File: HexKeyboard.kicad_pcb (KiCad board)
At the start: 2 copper layers, 66.8 x 99.3 mm, 37 parts, among them J3 Conn_02x04_Odd_Even, J5 USB_A, SW1 SW_3, SW10 SW_9, SW11 SW_8, SW12 SW_7, SW13 SW_Hash, SW14 SW_Hash, SW15 SW_0, SW16 SW_Star, SW17 SW_Hash, SW18 SW_Hash, SW19 SW_0, SW2 SW_3, SW20 SW_Star, SW3 SW_2, SW4 SW_1, SW5 SW_6, SW6 SW_6, SW7 SW_5, SW8 SW_4, SW9 SW_9, U2 74LVC125, U4 AT24CS64-XHM, Y1 16MHz

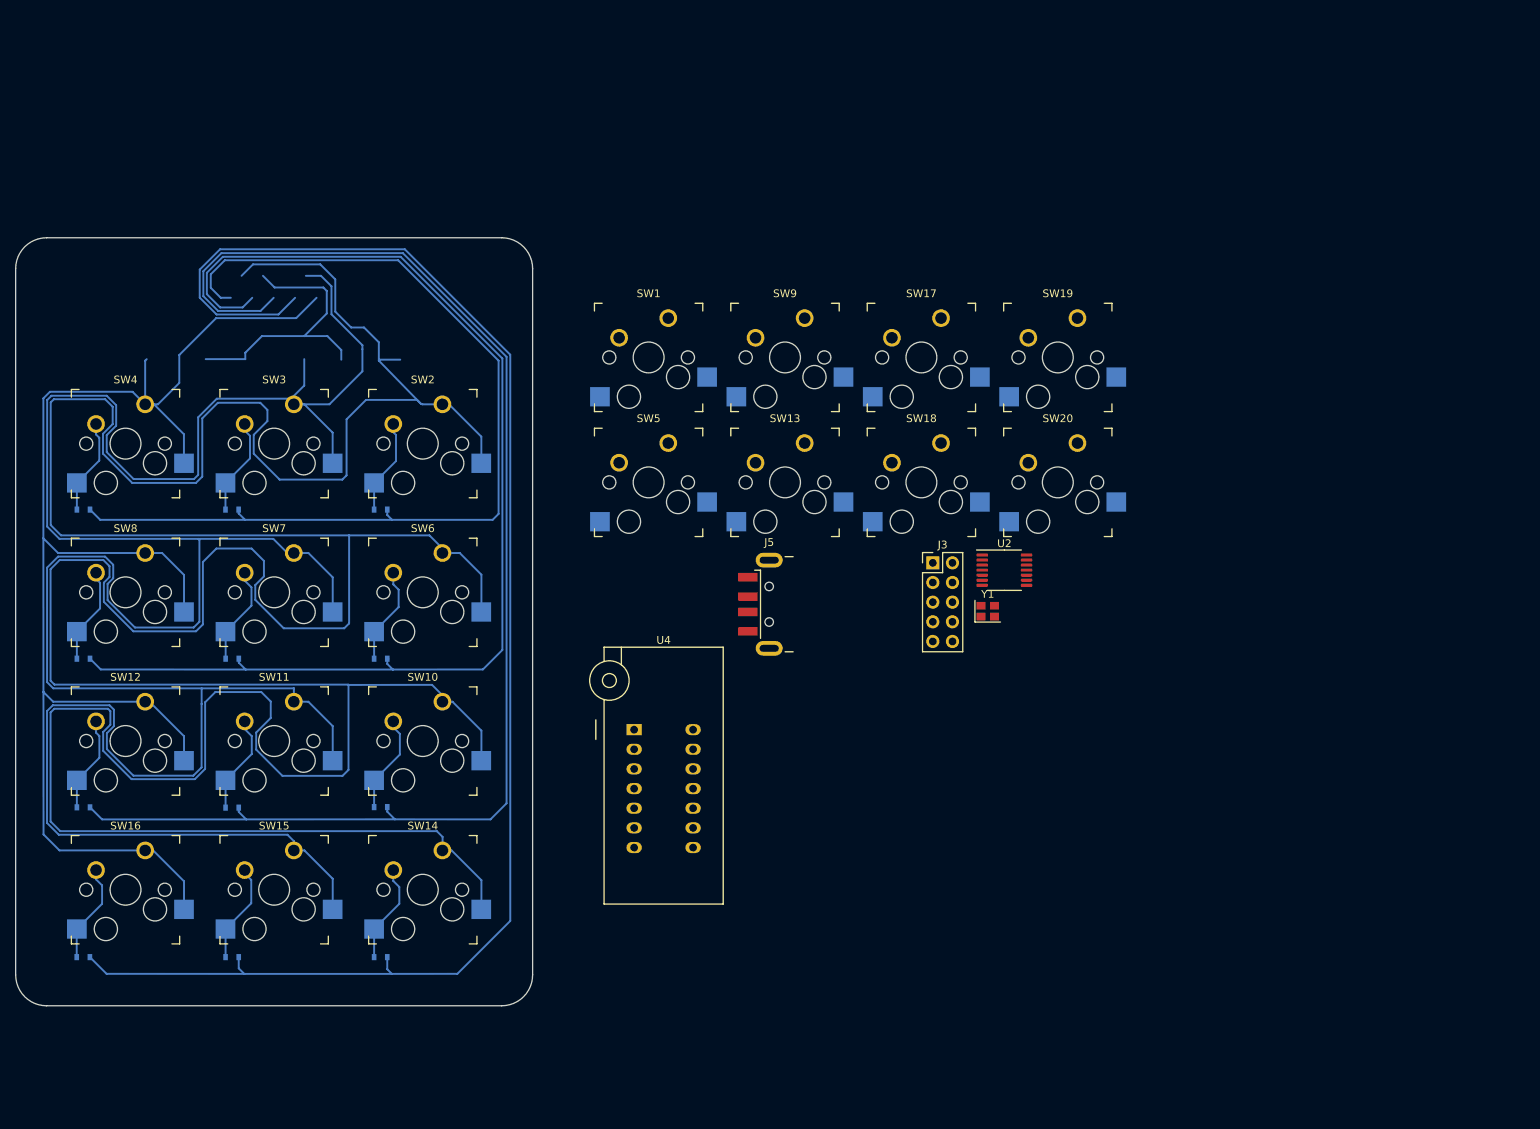
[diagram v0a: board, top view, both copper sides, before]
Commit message: Cleaned up libraries Added Display Switched to USB-C
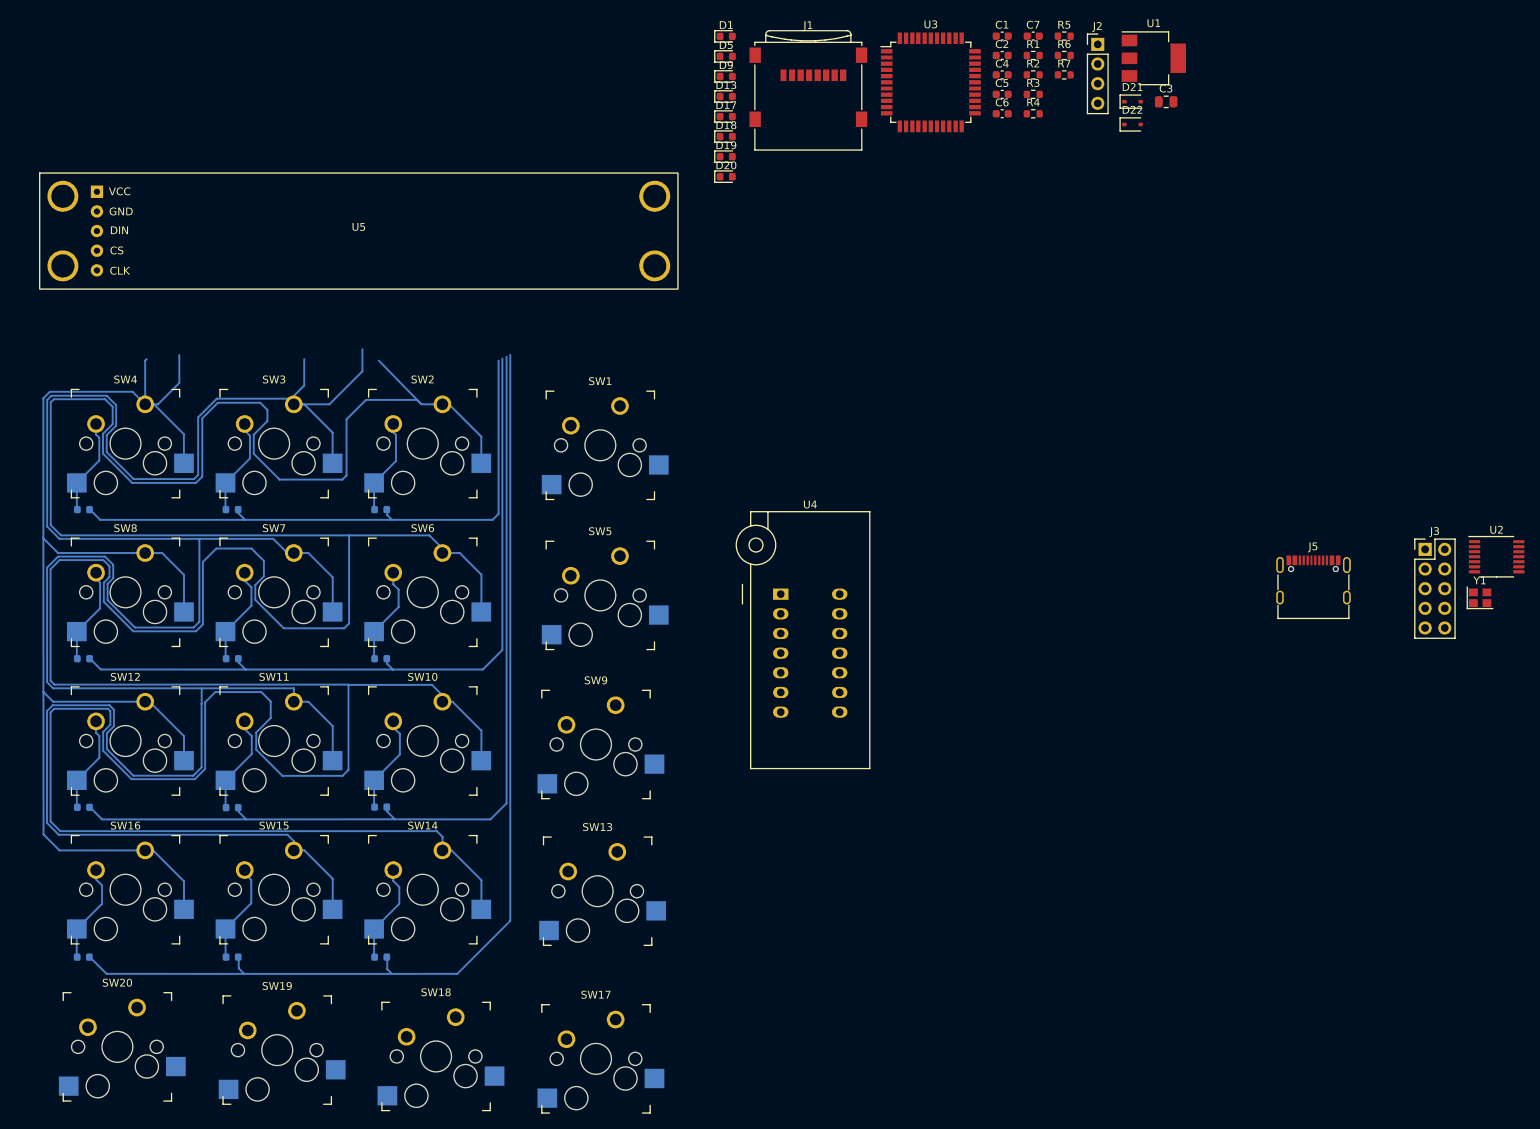
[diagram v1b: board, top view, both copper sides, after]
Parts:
- added C1: 100nF, Capacitor_SMD:C_0603_1608Metric, F.Cu at (209.5, 34.6)
- added C2: 100nF, Capacitor_SMD:C_0603_1608Metric, F.Cu at (209.5, 37.2)
- added C3: 10uF/10V, Capacitor_SMD:C_0805_2012Metric, F.Cu at (230.7, 43.1)
- added C4: 100nF, Capacitor_SMD:C_0603_1608Metric, F.Cu at (209.5, 39.7)
- added C5: 9pF, Capacitor_SMD:C_0603_1608Metric, F.Cu at (209.5, 42.2)
- added C6: 9pF, Capacitor_SMD:C_0603_1608Metric, F.Cu at (209.5, 44.7)
- added C7: 1uF, Capacitor_SMD:C_0603_1608Metric, F.Cu at (213.5, 34.6)
- added D1: D, Diode_SMD:D_0603_1608Metric, F.Cu at (173.9, 34.7)
- added D13: D, Diode_SMD:D_0603_1608Metric, F.Cu at (173.9, 42.5)
- added D17: D, Diode_SMD:D_0603_1608Metric, F.Cu at (173.9, 45.0)
- added D18: D, Diode_SMD:D_0603_1608Metric, F.Cu at (173.9, 47.6)
- added D19: D, Diode_SMD:D_0603_1608Metric, F.Cu at (173.9, 50.2)
- added D20: D, Diode_SMD:D_0603_1608Metric, F.Cu at (173.9, 52.8)
- added D21: BZX384-xxx, Diode_SMD:D_SOD-323, F.Cu at (226.4, 43.1)
- added D22: BZX384-xxx, Diode_SMD:D_SOD-323, F.Cu at (226.4, 46.1)
- added D5: D, Diode_SMD:D_0603_1608Metric, F.Cu at (173.9, 37.3)
- added D9: D, Diode_SMD:D_0603_1608Metric, F.Cu at (173.9, 39.9)
- added J1: Micro_SD_Card, Connector_Card:microSD_HC_Wuerth_693072010801, F.Cu at (184.5, 41.3)
- added J2: Conn_01x04, Connector_PinHeader_2.54mm:PinHeader_1x04_P2.54mm_Vertical, F.Cu at (221.9, 35.7)
- added R1: 3k3, Resistor_SMD:R_0603_1608Metric, F.Cu at (213.5, 37.2)
- added R2: 3k3, Resistor_SMD:R_0603_1608Metric, F.Cu at (213.5, 39.7)
- added R3: 3k3, Resistor_SMD:R_0603_1608Metric, F.Cu at (213.5, 42.2)
- added R4: 22, Resistor_SMD:R_0603_1608Metric, F.Cu at (213.5, 44.7)
- added R5: 22, Resistor_SMD:R_0603_1608Metric, F.Cu at (217.5, 34.6)
- added R6: 5k6, Resistor_SMD:R_0603_1608Metric, F.Cu at (217.5, 37.2)
- added R7: 5k6, Resistor_SMD:R_0603_1608Metric, F.Cu at (217.5, 39.7)
- added U1: AMS1117-3.3, Package_TO_SOT_SMD:SOT-223-3_TabPin2, F.Cu at (229.1, 37.5)
- added U3: ATmega32U4-AU, Package_QFP:TQFP-44_10x10mm_P0.8mm, F.Cu at (200.3, 40.6)
- added U5: MAX7219, MyFootprints:Display_x8_MAX7219, F.Cu at (126.4, 59.8)
- D10, D11, D12, D14, D15, D16, D2, D3, D4, D6, D7, D8: footprint Diodes_SMD:D_0603 -> Diode_SMD:D_0603_1608Metric
- J5: footprint Connector_USB:USB_A_CNCTech_1001-011-01101_Horizontal -> Connector_USB:USB_C_Receptacle_G-Switch_GT-USB-7010ASV
- moved SW20 141.8 mm to (97.7, 160.2)
- moved SW19 134.9 mm to (118.4, 160.6)
- moved SW17 99.9 mm to (159.6, 161.8)
- moved SW18 97.2 mm to (138.9, 161.4)
- moved Y1 63.7 mm to (271.3, 107.2)
- moved J3 63.7 mm to (264.2, 101.0)
- moved U2 63.7 mm to (273.4, 101.9)
- moved J5 63.5 mm to (249.8, 106.1)
- moved SW13 58.1 mm to (159.8, 140.1)
- moved SW9 55.7 mm to (159.6, 121.1)
- moved U4 25.8 mm to (180.9, 106.8)
- moved SW5 15.9 mm to (160.1, 101.9)
- moved SW1 13.0 mm to (160.1, 82.5)
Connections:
- net /COL0 renamed COL0
- net /COL1 renamed COL1
- net /COL2 renamed COL2
- net /COL3 renamed COL3
- net /ROW0 renamed ROW0
- net /ROW1 renamed ROW1
- net /ROW2 renamed ROW2
- net /ROW3 renamed ROW3
- U2 pad 11: +3.3V -> unconnected-(U2-Pad11)
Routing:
- net ROW3: track 200.8 -> 136.1 mm
- net ROW2: track 176.5 -> 117.0 mm
- net ROW1: track 150.5 -> 96.2 mm
- net ROW0: track 124.9 -> 76.7 mm
- net (no net): track 37.4 -> 0.00 mm
- net COL1: track 525.2 -> 495.0 mm
- net COL3: track 189.7 -> 168.9 mm
- net COL2: track 352.6 -> 338.9 mm
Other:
- board outline removed
- board text removed: "Atari 2600 keypad replica for Cherry MX switches or Kailh sockets January 2021 Hans@Liss.nu"
- board text removed: "Horizontal: SW{1,2,3} = JOY0 SW{4,5,6} = JOY1 SW{7,8,9} = JOY2 SW{10,11,12} = JOY3 Vertical: SW{1,4,7,10} = POTY, 4k7 pullup SW{2,5,8,11} = POTX, 4k7 pullup SW{3,6,9,12} = BUTTON"

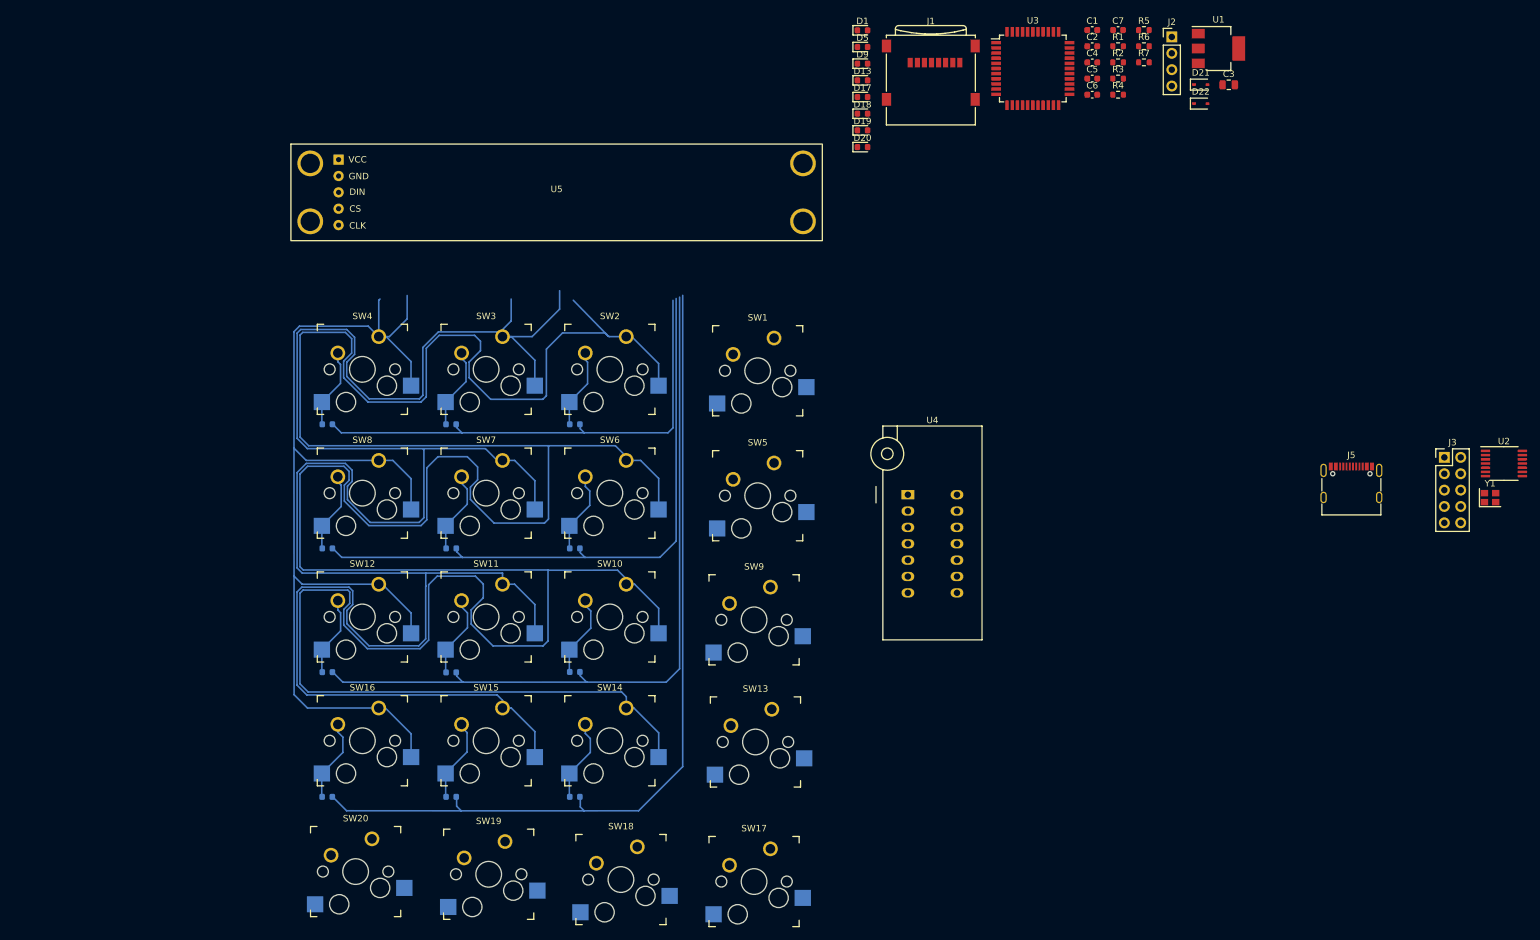
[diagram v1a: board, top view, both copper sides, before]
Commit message: Filled up matrix to 5x5 Started on layout
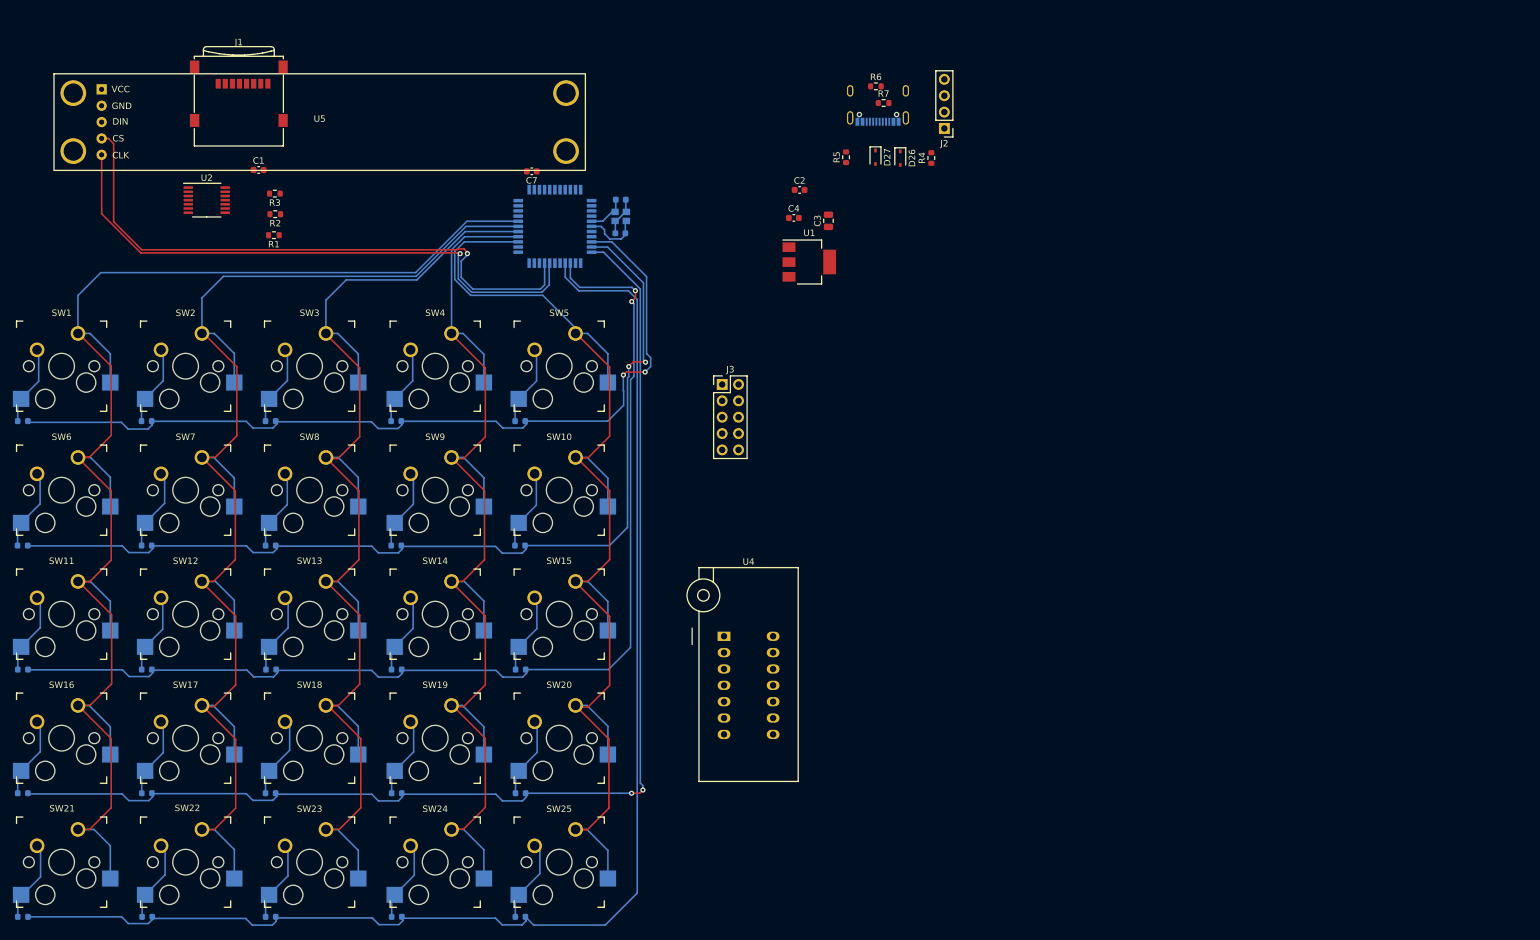
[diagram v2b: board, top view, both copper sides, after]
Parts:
- added D10: D, Diode_SMD:D_0603_1608Metric, B.Cu at (120.7, 114.7)
- added D15: D, Diode_SMD:D_0603_1608Metric, B.Cu at (120.8, 133.9)
- added D20: D, Diode_SMD:D_0603_1608Metric, B.Cu at (120.8, 153.1)
- added D25: D, Diode_SMD:D_0603_1608Metric, B.Cu at (120.7, 172.3)
- added D5: D, Diode_SMD:D_0603_1608Metric, B.Cu at (120.7, 95.4)
- added SW10: SW_10, keyswitches:Kailh_socket_MX_optional_compatible, F.Cu at (129.3, 101.0)
- added SW15: SW_15, keyswitches:Kailh_socket_MX_optional_compatible, F.Cu at (129.3, 120.2)
- added SW20: SW_20, keyswitches:Kailh_socket_MX_optional_compatible, F.Cu at (129.3, 139.5)
- added SW25: SW_25, keyswitches:Kailh_socket_MX_optional_compatible, F.Cu at (129.3, 158.8)
- added SW5: SW_5, keyswitches:Kailh_socket_MX_optional_compatible, F.Cu at (129.3, 81.8)
- C5, C6, D1, J5, U3, Y1: moved to B.Cu
- D11: renamed from D9; moved to B.Cu
- D16: renamed from D13; moved to B.Cu
- D21: renamed from D17; moved to B.Cu
- D22: renamed from D18; moved to B.Cu
- D23: renamed from D19; moved to B.Cu
- D24: renamed from D20; moved to B.Cu
- D6: renamed from D5; moved to B.Cu
- SW1: value SW_3 -> SW_1
- SW11: renamed from SW9; value SW_9 -> SW_11
- SW12: renamed from SW10; value SW_9 -> SW_12
- SW13: renamed from SW11; value SW_8 -> SW_13
- SW14: renamed from SW12; value SW_7 -> SW_14
- SW16: renamed from SW13; value SW_Hash -> SW_16
- SW17: renamed from SW14; value SW_Hash -> SW_17
- SW18: renamed from SW15; value SW_0 -> SW_18
- SW19: renamed from SW16; value SW_Star -> SW_19
- SW2: value SW_3 -> SW_2
- SW21: renamed from SW17; value SW_Hash -> SW_21
- SW22: renamed from SW18; value SW_Hash -> SW_22
- SW23: renamed from SW19; value SW_0 -> SW_23
- SW24: renamed from SW20; value SW_Star -> SW_24
- SW3: value SW_2 -> SW_3
- SW4: value SW_1 -> SW_4
- SW7: renamed from SW6; value SW_6 -> SW_7
- SW8: renamed from SW7; value SW_5 -> SW_8
- SW9: renamed from SW8; value SW_4 -> SW_9
- moved U2 205.5 mm to (72.0, 61.0)
- moved D21 182.2 mm to (43.5, 172.3), turned to 180 degrees
- moved D16 171.0 mm to (43.5, 153.1), turned to 180 degrees
- moved D22 167.0 mm to (62.8, 172.3), turned to 180 degrees
- moved D11 160.8 mm to (43.5, 133.9), turned to 180 degrees
- moved D23 152.8 mm to (82.0, 172.3), turned to 180 degrees
- moved D6 151.6 mm to (43.5, 114.7), turned to 180 degrees
- moved D1 143.8 mm to (43.5, 95.4), turned to 180 degrees
- moved Y1 141.9 mm to (136.3, 63.6), turned to 180 degrees
- moved D24 139.7 mm to (101.5, 172.3), turned to 180 degrees
- moved R1 134.3 mm to (82.5, 66.5), turned to 180 degrees
- moved R2 133.0 mm to (82.7, 63.2), turned to 180 degrees
- moved R3 132.1 mm to (82.6, 60.0), turned to 180 degrees
- moved C1 131.2 mm to (80.1, 56.4)
- moved J3 112.7 mm to (152.1, 89.7)
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- renumbered D10 to D12, D11 to D13, D12 to D14, D14 to D17, D15 to D18, D16 to D19, D21 to D26, D22 to D27, D6 to D7, D7 to D8, D8 to D9, SW5 to SW6
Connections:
- U3 pad 36: COL3 -> COL4
- U3 pad 37: COL2 -> COL3
- U3 pad 38: COL1 -> COL2
- U3 pad 39: COL0 -> COL1
- U3 pad 40: unconnected-(U3-PF1-Pad40) -> COL0
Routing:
- net COL1: track 495.0 -> 211.6 mm
- net COL0: track 0.00 -> 231.7 mm
- net ROW4: track 0.00 -> 208.5 mm
- net COL4: track 0.00 -> 189.7 mm
- net COL2: track 338.9 -> 191.6 mm
- net Net-(U3-PB6): track 0.00 -> 93.0 mm, vias 0 -> 1
- net Net-(U3-PB5): track 0.00 -> 90.3 mm, vias 0 -> 1
- net ROW0: track 76.7 -> 132.4 mm, vias 0 -> 2
- net ROW1: track 96.2 -> 149.5 mm, vias 0 -> 2
- net ROW3: track 136.1 -> 187.9 mm, vias 0 -> 2
- net ROW2: track 117.0 -> 168.6 mm, vias 0 -> 2
- net Net-(D25-A): track 0.00 -> 12.9 mm
- net Net-(D21-A): track 0.00 -> 12.9 mm
- net Net-(D11-A): track 0.00 -> 12.8 mm
- net Net-(D6-A): track 0.00 -> 12.8 mm
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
